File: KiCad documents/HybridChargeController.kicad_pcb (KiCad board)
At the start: 2 copper layers, 90 parts, among them P1 Load, P2 LI_balancer, P3 PV, P4 Extra, P5 LI, P6 LA, Q1 MMBT3904, Q10 MMBT3904, Q11 IPD90P04P4L-04, Q12 STL60P4LLF6, Q13 STL60P4LLF6, Q2 IPD90P04P4L-04, Q3 RQ3E100BNTB, Q4 IPD90P04P4L-04, Q5 RQ3E100BNTB, Q6 MMBT3904, Q7 BSS138, Q8 MMBT3904, Q9 IPD90P04P4L-04, U1 LM358D, U2 bq76920, U3 cd4051, U4 LM358D, U5 LM358D

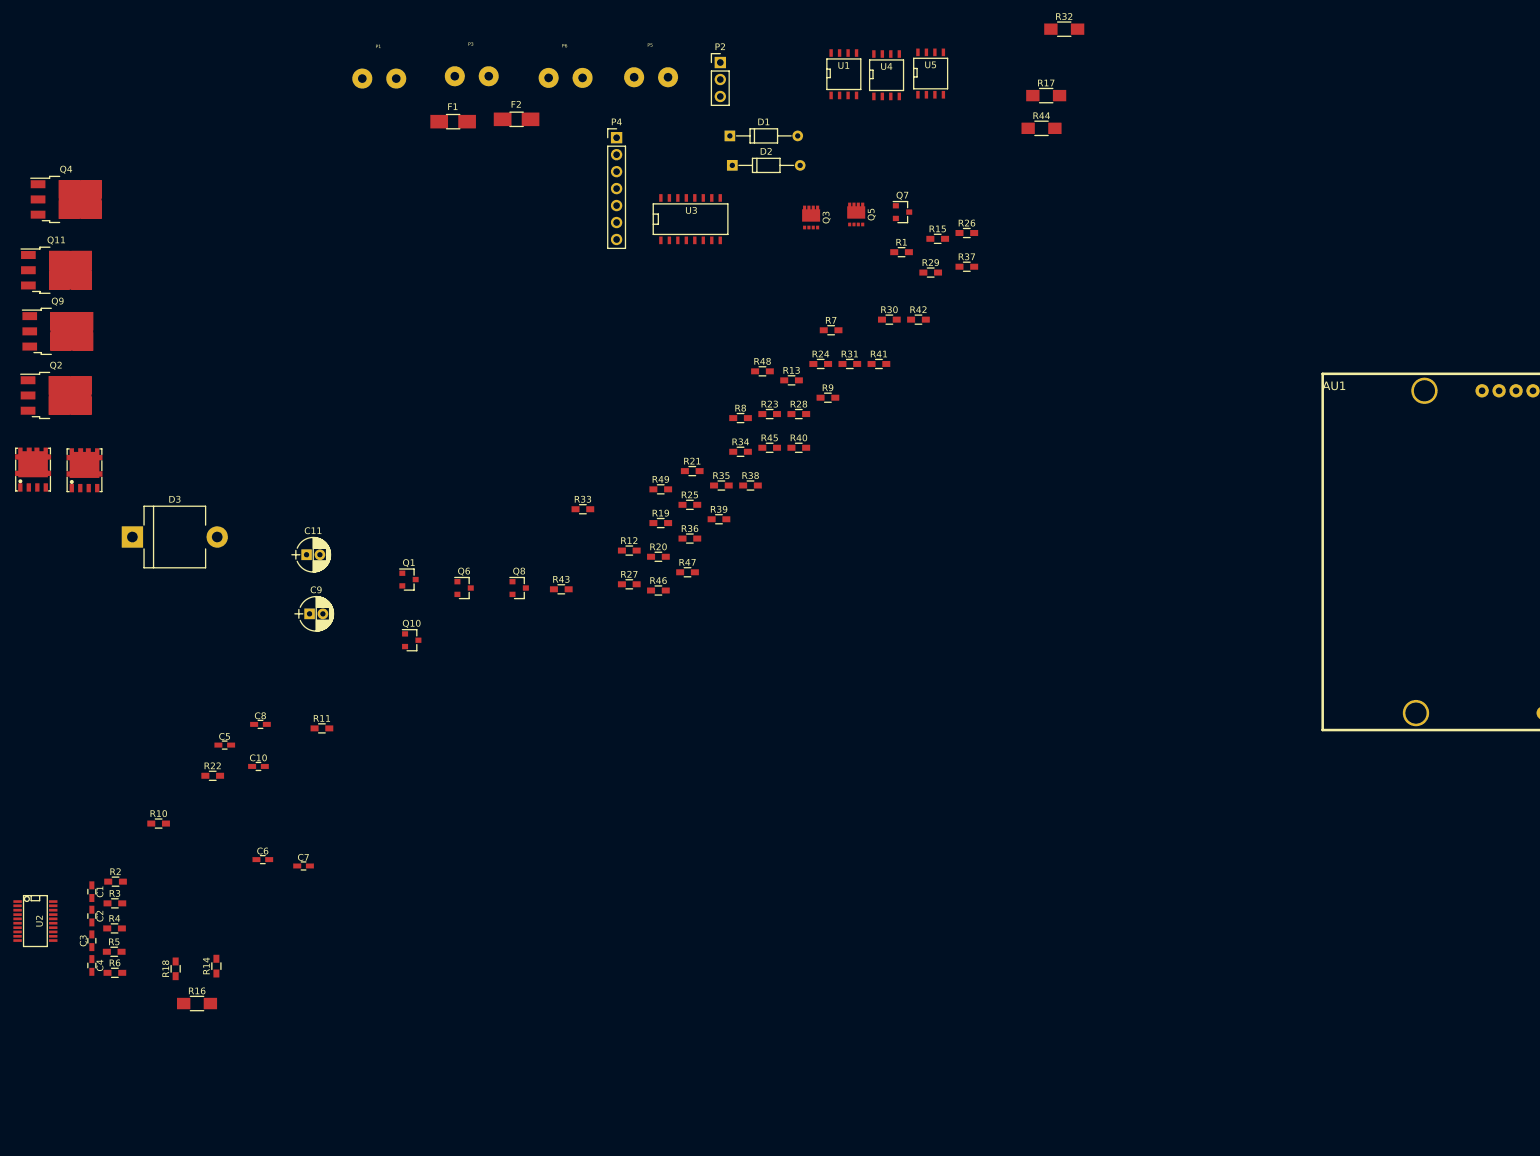
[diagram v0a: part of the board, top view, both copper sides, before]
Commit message: noticed low side switching
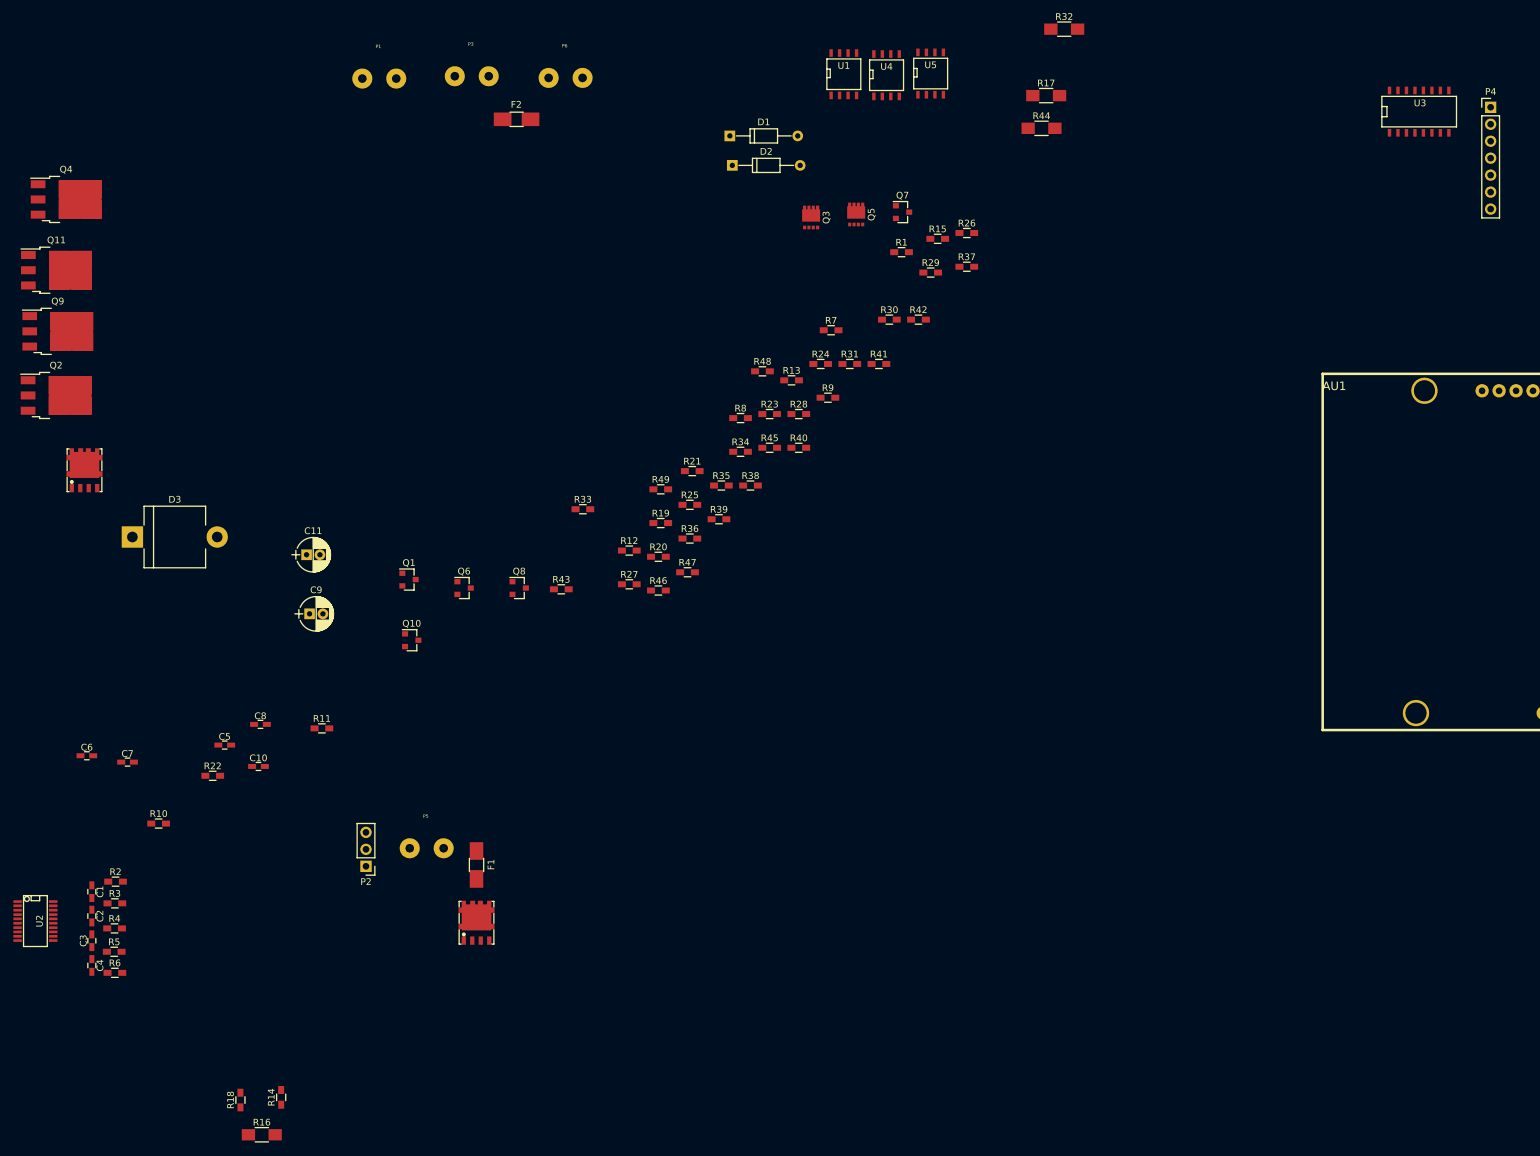
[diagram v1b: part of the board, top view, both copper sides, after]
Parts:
- moved P2 131.5 mm to (75.0, 141.7), turned to 180 degrees
- moved P4 131.0 mm to (243.4, 28.1)
- moved P5 120.2 mm to (81.6, 139.0)
- moved F1 111.4 mm to (91.6, 141.5), turned to 270 degrees
- moved U3 110.3 mm to (232.8, 28.7)
- moved Q12 94.9 mm to (91.6, 150.2)
- moved C7 30.6 mm to (39.4, 126.1)
- moved C6 30.6 mm to (33.2, 125.2)
- moved R14 21.9 mm to (62.4, 176.3)
- moved R16 21.9 mm to (59.5, 181.9)
- moved R18 21.9 mm to (56.2, 176.7)
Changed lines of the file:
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@@
     (links 218)
     (no_connects 202)
-    (area 0 0 0 0)
+    (area 20.095238 13.525 287.270501 165.225)
     (thickness 1.6)
     (drawings 0)
@@
     (pad_to_mask_clearance 0.2)
     (aux_axis_origin 0 0)
-    (visible_elements FFFEFF7F)
+    (visible_elements 7FFFFFFF)
     (pcbplotparams
       (layerselection 0x00030_80000001)
@@
   )
   (module Capacitors_SMD:C_0603_HandSoldering (layer F.Cu)
-    (at 59.6 140.7)
+    (at 33.25 125.15)
     (descr "Capacitor SMD 0603, hand soldering")
     (tags "capacitor 0603")
@@
   )
   (module Capacitors_SMD:C_0603_HandSoldering (layer F.Cu)
-    (at 65.7 141.65)
+    (at 39.35 126.1)
     (descr "Capacitor SMD 0603, hand soldering")
     (tags "capacitor 0603")
@@
   )
   (module Fuse_Holders_and_Fuses:Fuse_SMD1206_HandSoldering (layer F.Cu)
-    (at 88.1 30.2)
+    (at 91.6 141.5 270)
     (descr "Fuse, Sicherung, SMD1206, Littlefuse-Wickmann 433 Series, Hand Soldering,")
     (tags "Fuse Sicherung SMD1206 Littlefuse-Wickmann 433 Series Hand Soldering ")
     (attr smd)
-    (fp_text reference F1 (at -0.05 -2.2) (layer F.SilkS)
+    (fp_text reference F1 (at -0.05 -2.2 270) (layer F.SilkS)
       (effects (font (size 1 1) (thickness 0.15)))
     )
-    (fp_text value 15A (at -0.15 2.5) (layer F.Fab)
+    (fp_text value 15A (at -0.15 2.5 270) (layer F.Fab)
       (effects (font (size 1 1) (thickness 0.15)))
     )
@@
     (fp_line (start 3.35 1.58) (end 3.35 -1.58) (layer F.CrtYd) (width 0.05))
     (fp_line (start 3.35 1.58) (end -3.35 1.58) (layer F.CrtYd) (width 0.05))
-    (pad 1 smd rect (at -2.09 0 90) (size 2.03 2.65) (layers F.Cu F.Paste F.Mask)
+    (pad 1 smd rect (at -2.09 0) (size 2.03 2.65) (layers F.Cu F.Paste F.Mask)
       (net 41 "Net-(F1-Pad1)"))
-    (pad 2 smd rect (at 2.09 0 90) (size 2.03 2.65) (layers F.Cu F.Paste F.Mask)
+    (pad 2 smd rect (at 2.09 0) (size 2.03 2.65) (layers F.Cu F.Paste F.Mask)
       (net 42 "Net-(F1-Pad2)"))
   )
@@
   )
   (module Pin_Headers:Pin_Header_Straight_1x03_Pitch2.54mm (layer F.Cu)
-    (at 128.1 21.35)
+    (at 75.05 141.7 180)
     (descr "Through hole straight pin header, 1x03, 2.54mm pitch, single row")
     (tags "Through hole pin header THT 1x03 2.54mm single row")
-    (fp_text reference P2 (at 0 -2.33) (layer F.SilkS)
+    (fp_text reference P2 (at 0 -2.33 180) (layer F.SilkS)
       (effects (font (size 1 1) (thickness 0.15)))
     )
-    (fp_text value LI_balancer (at 0 7.41) (layer F.Fab)
+    (fp_text value LI_balancer (at 0 7.41 180) (layer F.Fab)
       (effects (font (size 1 1) (thickness 0.15)))
     )
@@
     (fp_line (start 1.8 6.85) (end 1.8 -1.8) (layer F.CrtYd) (width 0.05))
     (fp_line (start 1.8 -1.8) (end -1.8 -1.8) (layer F.CrtYd) (width 0.05))
-    (fp_text user %R (at 0 -2.33) (layer F.Fab)
+    (fp_text user %R (at 0 -2.33 180) (layer F.Fab)
       (effects (font (size 1 1) (thickness 0.15)))
     )
-    (pad 1 thru_hole rect (at 0 0) (size 1.7 1.7) (drill 1) (layers *.Cu *.Mask)
+    (pad 1 thru_hole rect (at 0 0 180) (size 1.7 1.7) (drill 1) (layers *.Cu *.Mask)
       (net 47 /CELL12))
-    (pad 2 thru_hole oval (at 0 2.54) (size 1.7 1.7) (drill 1) (layers *.Cu *.Mask)
+    (pad 2 thru_hole oval (at 0 2.54 180) (size 1.7 1.7) (drill 1) (layers *.Cu *.Mask)
       (net 48 /CELL23))
-    (pad 3 thru_hole oval (at 0 5.08) (size 1.7 1.7) (drill 1) (layers *.Cu *.Mask)
+    (pad 3 thru_hole oval (at 0 5.08 180) (size 1.7 1.7) (drill 1) (layers *.Cu *.Mask)
       (net 49 /CELL34))
     (model ${KISYS3DMOD}/Pin_Headers.3dshapes/Pin_Header_Straight_1x03_Pitch2.54mm.wrl
@@
   )
   (module Pin_Headers:Pin_Header_Straight_1x07_Pitch2.54mm (layer F.Cu)
-    (at 112.574762 32.605)
+    (at 243.45 28.05)
     (descr "Through hole straight pin header, 1x07, 2.54mm pitch, single row")
     (tags "Through hole pin header THT 1x07 2.54mm single row")
@@
   )
   (module VCS_library:TerminalBlock_Screw_2pol (layer F.Cu)
-    (at 115.2 23.55)
+    (at 81.6 139)
     (descr "2-way 5mm pitch terminal block, Phoenix MKDS series")
     (fp_text reference P5 (at 2.4 -4.8) (layer F.SilkS)
@@
   )
   (module bachelorSMDs:powerFLAT_5x6_5..8com (layer F.Cu)
-    (at 25.2 82.3)
+    (at 91.6 150.15)
     (fp_text reference Q12 (at 0 4.4) (layer F.Fab)
       (effects (font (size 1 1) (thickness 0.15)))
@@
   )
   (module Resistors_SMD:R_0603_HandSoldering (layer F.Cu)
-    (at 52.65 156.65 90)
+    (at 62.35 176.3 90)
     (descr "Resistor SMD 0603, hand soldering")
     (tags "resistor 0603")
@@
   )
   (module Resistors_SMD:R_1206_HandSoldering (layer F.Cu)
-    (at 49.75 162.25)
+    (at 59.45 181.9)
     (descr "Resistor SMD 1206, hand soldering")
     (tags "resistor 1206")
@@
   )
   (module Resistors_SMD:R_0603_HandSoldering (layer F.Cu)
-    (at 46.55 157.05 90)
+    (at 56.25 176.7 90)
     (descr "Resistor SMD 0603, hand soldering")
     (tags "resistor 0603")
@@
   )
   (module SMD_Packages:SO-16-N (layer F.Cu)
-    (at 123.65 44.8)
+    (at 232.75 28.7)
     (descr "Module CMS SOJ 16 pins large")
     (tags "CMS SOJ")

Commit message: startet distributing components
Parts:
- removed D1: 1N4148-T, Diodes_ThroughHole:D_DO-35_SOD27_P10.16mm_Horizontal
- added Q14: IPD90P04P4L-04, TO_SOT_Packages_SMD:TO-252-3_TabPin2, F.Cu at (58.4, 158.6)
- added R50: 47k, Resistors_SMD:R_0603_HandSoldering, F.Cu at (71.6, 166.4)
- added R51: 100k, Resistors_SMD:R_0603_HandSoldering, F.Cu at (58.7, 172.4)
- added R52: 47k, Resistors_SMD:R_0603_HandSoldering, F.Cu at (58.4, 166.5)
- Q3: value RQ3E100BNTB -> MMBT3904; footprint bachelorSMDs:HSMT-8 -> TO_SOT_Packages_SMD:SOT-23
- Q5: value RQ3E100BNTB -> IPD90P04P4L-04; footprint bachelorSMDs:HSMT-8 -> TO_SOT_Packages_SMD:TO-252-3_TabPin2
- Q7: value BSS138 -> MMBT3904
- R22, R33: value 1M -> 10k
- R28: value 1M -> 100k
- moved Q7 158.5 mm to (58.8, 169.4), turned to 90 degrees
- moved R13 147.2 mm to (20.4, 156.4), turned to 180 degrees
- moved Q3 144.6 mm to (70.6, 170.4), turned to 90 degrees
- moved Q5 137.9 mm to (71.3, 158.4), turned to 90 degrees
- moved R17 131.9 mm to (47.9, 53.6), turned to 90 degrees
- moved R28 121.1 mm to (70.6, 173.3), turned to 180 degrees
- moved R15 116.5 mm to (44.2, 49.7), turned to 180 degrees
- moved R29 115.9 mm to (275.2, 61.5)
- moved R41 115.9 mm to (267.4, 75.2)
- moved R1 115.9 mm to (270.8, 58.5)
- moved R31 115.9 mm to (263.0, 75.2)
- moved R34 115.9 mm to (246.7, 88.4)
- moved R38 115.9 mm to (248.2, 93.4)
- moved R39 115.9 mm to (243.5, 98.5)
- moved R40 115.9 mm to (255.4, 87.8)
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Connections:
- C7 pad 1: /LI+ -> /5V
- Q3 pad 2: Net-(Q3-Pad1) -> /GND
- Q3 pad 3: Net-(Q3-Pad1) -> Net-(Q3-Pad3)
- Q5 pad 1: /GND -> Net-(Q3-Pad3)
- Q5 pad 2: /GND -> /LI+
- Q5 pad 3: /GND -> Net-(Q14-Pad3)
- Q7 pad 1: /GND -> Net-(Q7-Pad1)
- Q7 pad 2: Net-(D1-Pad2) -> /GND
- Q7 pad 3: /CHG -> Net-(Q14-Pad1)
- R16 pad 1: Net-(Q3-Pad1) -> /GND
- R18 pad 1: Net-(Q3-Pad1) -> /GND
- R22 pad 1: /DSG -> Net-(Q3-Pad1)
- R22 pad 2: Net-(Q3-Pad1) -> /CHG
- R28 pad 1: Net-(D1-Pad2) -> /GND
- R28 pad 2: Net-(D1-Pad1) -> Net-(Q3-Pad1)
- R33 pad 1: Net-(D1-Pad1) -> Net-(Q7-Pad1)
- R33 pad 2: /GND -> /DSG
- U2 pad 9: /LI+ -> /5V

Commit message: completed vaguely arranging footprints
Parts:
- moved C7 198.4 mm to (214.1, 166.0), turned to 270 degrees
- moved C6 195.6 mm to (211.1, 165.8), turned to 0 degrees
- moved P3 195.1 mm to (270.4, 93.8)
- moved C9 192.9 mm to (211.1, 161.1), turned to 0 degrees
- moved R13 187.9 mm to (207.6, 171.9), turned to 0 degrees
- moved Q4 182.5 mm to (241.3, 102.0), turned to 0 degrees
- moved R10 181.2 mm to (204.8, 159.3), turned to 180 degrees
- moved P6 180.4 mm to (220.9, 89.0)
- moved R15 180.4 mm to (218.3, 97.0)
- moved R19 180.4 mm to (210.1, 109.7)
- moved R21 180.4 mm to (219.3, 106.0)
- moved R24 180.4 mm to (216.9, 112.8)
- moved R7 180.4 mm to (225.1, 93.9)
- moved U1 180.4 mm to (211.7, 103.0)
- moved F2 180.4 mm to (232.9, 93.0)
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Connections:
- AU1 pad 8: /D8 -> /SW_PV
- D3 pad 1: /COM+ -> /PV+
- P1 pad 1: /LOAD+ -> /LOAD-
- P1 pad 2: /LOAD- -> /LOAD+
- P3 pad 1: Net-(D3-Pad2) -> /PV-
- P3 pad 2: /PV- -> Net-(D3-Pad2)
- Q11 pad 3: /COM+ -> /PV+
- R40 pad 2: /COM+ -> /PV+
- R41 pad 1: /COM+ -> /PV+

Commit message: power paths done
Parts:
- added Q15: BSS138, TO_SOT_Packages_SMD:SOT-23, F.Cu at (138.0, 117.0)
- added Q16: BSS138, TO_SOT_Packages_SMD:SOT-23, F.Cu at (138.0, 110.0)
- added R53: 10k, Resistors_SMD:R_0603_HandSoldering, F.Cu at (135.0, 117.0)
- added R54: 10k, Resistors_SMD:R_0603_HandSoldering, F.Cu at (141.0, 117.0)
- added R55: 10k, Resistors_SMD:R_0603_HandSoldering, F.Cu at (135.0, 110.0)
- added R56: 10k, Resistors_SMD:R_0603_HandSoldering, F.Cu at (141.0, 110.0)
- added REF**: Screwhole, Screwholes:Screwhole, F.Cu at (103.5, 45.4)
- added REF**: Screwhole, Screwholes:Screwhole, F.Cu at (181.6, 43.6)
- AU1: footprint Arduinos:ARDUINO_SHIELD_bigger_holes -> Arduinos:ARDUINO_SHIELD_bigger_holes_no_outline
- P4: footprint Pin_Headers:Pin_Header_Straight_1x07_Pitch2.54mm -> Pin_Headers:Pin_Header_Straight_1x06_Pitch2.54mm
- Q13: footprint bachelorSMDs:powerFLAT_5x6_5..8com -> powerFLAT_5x6_5..8com
- moved P4 140.2 mm to (142.8, 83.8), turned to 90 degrees
- moved AU1 120.2 mm to (113.7, 125.1)
- moved C11 119.8 mm to (159.3, 118.0)
- moved D2 116.3 mm to (163.2, 113.2)
- moved R40 113.7 mm to (171.5, 63.5)
- moved Q10 113.2 mm to (167.2, 64.0)
- moved Q11 113.2 mm to (171.2, 56.5)
- moved R44 113.2 mm to (165.7, 46.6)
- moved R43 112.2 mm to (163.3, 41.8)
- moved P3 111.6 mm to (170.0, 45.0)
- moved D3 111.0 mm to (181.6, 63.5)
- moved R41 110.9 mm to (173.9, 65.7)
- moved R42 110.0 mm to (169.3, 67.2)
- moved R39 109.3 mm to (165.7, 69.0)
- moved R38 108.4 mm to (162.2, 69.0)
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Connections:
- AU1 pad 3V3: Net-(AU1-Pad3V3) -> /3.3V
- AU1 pad A4: /SDA -> /SDA5
- AU1 pad A5: /SCL -> /SCL5
- P4 pad 4: /D5 -> /LED_BTN
- P4 pad 5: /D8 -> /D9
- P4 pad 6: /D9 -> /RST
- U2 pad 4: /SDA -> /SDA3
- U2 pad 5: /SCL -> /SCL3
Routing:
- net /COM+: track 0.00 -> 85.6 mm
- net /GND: track 0.00 -> 13.0 mm, vias 0 -> 4
- net /LI+: track 0.00 -> 10.5 mm
- net /LOAD-: track 0.00 -> 8.92 mm
- net Net-(D3-Pad2): track 0.00 -> 8.85 mm
- net Net-(F1-Pad2): track 0.00 -> 8.66 mm
- net /PV+: track 0.00 -> 8.18 mm
- net Net-(F1-Pad1): track 0.00 -> 7.70 mm
- net /LA+: track 0.00 -> 7.40 mm
- net /LOAD+: track 0.00 -> 7.32 mm
- net Net-(Q14-Pad3): track 0.00 -> 6.44 mm
- net /PV-: track 0.00 -> 6.30 mm
- net Net-(F2-Pad1): track 0.00 -> 6.10 mm
- net /LA-: track 0.00 -> 5.34 mm
- net Net-(Q4-Pad3): track 0.00 -> 5.11 mm
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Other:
- board outline added: 87 x 87 mm

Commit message: more traces done
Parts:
- P4: footprint Pin_Headers:Pin_Header_Straight_1x06_Pitch2.54mm -> Pin_Headers:Pin_Header_Straight_1x05_Pitch2.54mm
- Q13: footprint powerFLAT_5x6_5..8com -> bachelorSMDs:powerFLAT_5x6_5..8com
- moved R2 9.80 mm to (117.8, 102.0), turned to 0 degrees
- moved R33 5.93 mm to (135.0, 97.0), turned to 270 degrees
- moved R22 5.87 mm to (132.0, 101.5), turned to 270 degrees
- moved R51 4.53 mm to (135.0, 91.0)
- moved R25 2.85 mm to (145.5, 56.0)
- moved R30 2.85 mm to (145.0, 63.0)
- moved R12 2.77 mm to (118.5, 55.5)
- moved R23 2.69 mm to (130.0, 59.5), turned to 180 degrees
- moved R21 2.61 mm to (130.0, 50.5), turned to 0 degrees
- moved R37 2.07 mm to (149.5, 63.0)
- moved Q8 1.90 mm to (142.5, 59.0)
- moved R35 1.80 mm to (139.8, 59.0)
- moved U5 1.73 mm to (110.0, 62.0)
- moved Q1 1.60 mm to (116.5, 51.5)
- moved R20 1.29 mm to (130.0, 56.5), turned to 0 degrees
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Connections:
- AU1 pad 9: /D9 -> /Alert
- P4 pad 5: /D9 -> /RST
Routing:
- net /S_LD_I: track 0.00 -> 61.7 mm, vias 0 -> 5
- net /LI-: track 4.99 -> 60.1 mm
- net /5V: track 0.00 -> 42.0 mm
- net /3.3V: track 0.00 -> 28.5 mm, vias 0 -> 2
- net /COM+: track 85.6 -> 114.0 mm
- net /SRN: track 0.00 -> 25.8 mm, vias 0 -> 2
- net /DSG: track 0.00 -> 24.6 mm, vias 0 -> 2
- net /SRP: track 0.00 -> 23.4 mm, vias 0 -> 2
- net /LI+: track 10.5 -> 32.7 mm
- net Net-(Q14-Pad1): track 0.00 -> 19.4 mm, vias 0 -> 2
- net /CHG: track 0.00 -> 17.7 mm, vias 0 -> 2
- net /VC1: track 0.00 -> 17.6 mm
- net /SCL3: track 0.00 -> 15.8 mm, vias 0 -> 2
- net Net-(Q14-Pad3): track 6.44 -> 21.9 mm
- net Net-(R34-Pad2): track 0.00 -> 14.7 mm
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
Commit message: almost all tracks done
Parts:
- moved D2 13.9 mm to (155.3, 101.7), turned to 90 degrees
- moved U3 11.0 mm to (170.0, 99.6)
- moved R48 5.28 mm to (168.0, 71.0)
- moved R46 5.24 mm to (185.2, 75.8), turned to 90 degrees
- moved R41 3.05 mm to (172.0, 68.0)
- moved R38 2.73 mm to (164.0, 71.0), turned to 0 degrees
- moved R49 2.00 mm to (172.0, 71.0), turned to 0 degrees
- moved R39 1.93 mm to (164.0, 68.0), turned to 180 degrees
- moved R40 1.63 mm to (172.0, 65.0)
- moved R43 1.54 mm to (162.0, 42.5)
- moved C11 1.53 mm to (159.0, 116.5)
- moved R42 1.50 mm to (168.0, 68.0)
- moved P4 1.48 mm to (144.0, 83.0)
- moved Q10 1.27 mm to (166.0, 64.2), turned to 90 degrees
- moved U4 1.10 mm to (179.0, 68.2)
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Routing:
- net /5V: track 42.0 -> 175.2 mm, vias 0 -> 10
- net /S_LA_V: track 0.00 -> 84.5 mm, vias 0 -> 4
- net /S_LA_I: track 0.00 -> 67.8 mm, vias 0 -> 10
- net /Alert: track 0.00 -> 66.7 mm, vias 0 -> 5
- net /COM+: track 114.0 -> 178.3 mm, vias 0 -> 4
- net /SW_LD: track 0.00 -> 63.1 mm, vias 0 -> 7
- net /MplexA: track 0.00 -> 58.9 mm
- net /MplexB: track 0.00 -> 52.0 mm
- net Net-(R43-Pad2): track 0.00 -> 49.1 mm, vias 0 -> 6
- net /MplexC: track 0.00 -> 43.9 mm
- net /RST: track 0.00 -> 42.7 mm, vias 0 -> 5
- net /SCL5: track 2.46 -> 44.5 mm, vias 0 -> 6
- net /PV-: track 6.30 -> 47.2 mm, vias 0 -> 2
- net /SDA5: track 2.46 -> 40.5 mm, vias 0 -> 6
- net /S_PV_I: track 0.00 -> 34.5 mm, vias 0 -> 2
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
